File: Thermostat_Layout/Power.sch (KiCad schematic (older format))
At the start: 8 parts, among them J2 Conn_01x02_Male, U3 TSR_1-2433

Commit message: Update schematic
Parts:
- renumbered R5 to R6, R6 to R7, U3 to U4
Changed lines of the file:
@@
 $EndDescr
 $Comp
-L power:+9V #PWR0101
+L power:+9V #PWR02
 U 1 1 5D3E58CF
 P 5500 2750
-F 0 "#PWR0101" H 5500 2600 50  0001 C CNN
+F 0 "#PWR02" H 5500 2600 50  0001 C CNN
 F 1 "+9V" H 5515 2923 50  0000 C CNN
 F 2 "" H 5500 2750 50  0001 C CNN
@@
 Connection ~ 5150 3000
 $Comp
-L Regulator_Switching:TSR_1-2433 U3
+L Regulator_Switching:TSR_1-2433 U4
 U 1 1 5D3E43BD
 P 6050 3100
-F 0 "U3" H 6050 3467 50  0000 C CNN
+F 0 "U4" H 6050 3467 50  0000 C CNN
 F 1 "TSR_1-2433" H 6050 3376 50  0000 C CNN
 F 2 "Converter_DCDC:Converter_DCDC_TRACO_TSR-1_THT" H 6050 2950 50  0001 L CIN
@@
 	5500 2750 5500 3000
 $Comp
-L SparkFun-PowerSymbols:GND #GND0103
+L SparkFun-PowerSymbols:GND #GND09
 U 1 1 5D3ED84A
 P 6050 3400
-F 0 "#GND0103" H 6100 3350 45  0001 L BNN
+F 0 "#GND09" H 6100 3350 45  0001 L BNN
 F 1 "GND" H 6050 3230 45  0000 C CNN
 F 2 "" H 6050 3300 60  0001 C CNN
@@
 	6050 3400 6050 3300
 $Comp
-L SparkFun-PowerSymbols:3.3V #SUPPLY0102
+L SparkFun-PowerSymbols:3.3V #SUPPLY06
 U 1 1 5D3EF310
 P 6600 2750
-F 0 "#SUPPLY0102" H 6650 2750 45  0001 L BNN
+F 0 "#SUPPLY06" H 6650 2750 45  0001 L BNN
 F 1 "3.3V" H 6600 3026 45  0000 C CNN
 F 2 "XXX-00000" H 6600 2931 60  0000 C CNN
@@
 	6600 2750 6600 3000
 $Comp
-L Device:R_US R5
+L Device:R_US R6
 U 1 1 5D3F0E01
 P 5350 4200
-F 0 "R5" H 5418 4246 50  0000 L CNN
+F 0 "R6" H 5418 4246 50  0000 L CNN
 F 1 "220k" H 5418 4155 50  0000 L CNN
 F 2 "Resistor_SMD:R_0402_1005Metric" V 5390 4190 50  0001 C CNN
@@
 $EndComp
 $Comp
-L Device:R_US R6
+L Device:R_US R7
 U 1 1 5D3F14FB
 P 5350 4500
-F 0 "R6" H 5418 4546 50  0000 L CNN
+F 0 "R7" H 5418 4546 50  0000 L CNN
 F 1 "100k" H 5418 4455 50  0000 L CNN
 F 2 "Resistor_SMD:R_0402_1005Metric" V 5390 4490 50  0001 C CNN
@@
 $EndComp
 $Comp
-L power:+9V #PWR0102
+L power:+9V #PWR01
 U 1 1 5D3F1ECA
 P 5350 4000
-F 0 "#PWR0102" H 5350 3850 50  0001 C CNN
+F 0 "#PWR01" H 5350 3850 50  0001 C CNN
 F 1 "+9V" H 5365 4173 50  0000 C CNN
 F 2 "" H 5350 4000 50  0001 C CNN
@@
 $EndComp
 $Comp
-L SparkFun-PowerSymbols:GND #GND0104
+L SparkFun-PowerSymbols:GND #GND08
 U 1 1 5D3F23F7
 P 5350 4700
-F 0 "#GND0104" H 5400 4650 45  0001 L BNN
+F 0 "#GND08" H 5400 4650 45  0001 L BNN
 F 1 "GND" H 5350 4530 45  0000 C CNN
 F 2 "" H 5350 4600 60  0001 C CNN

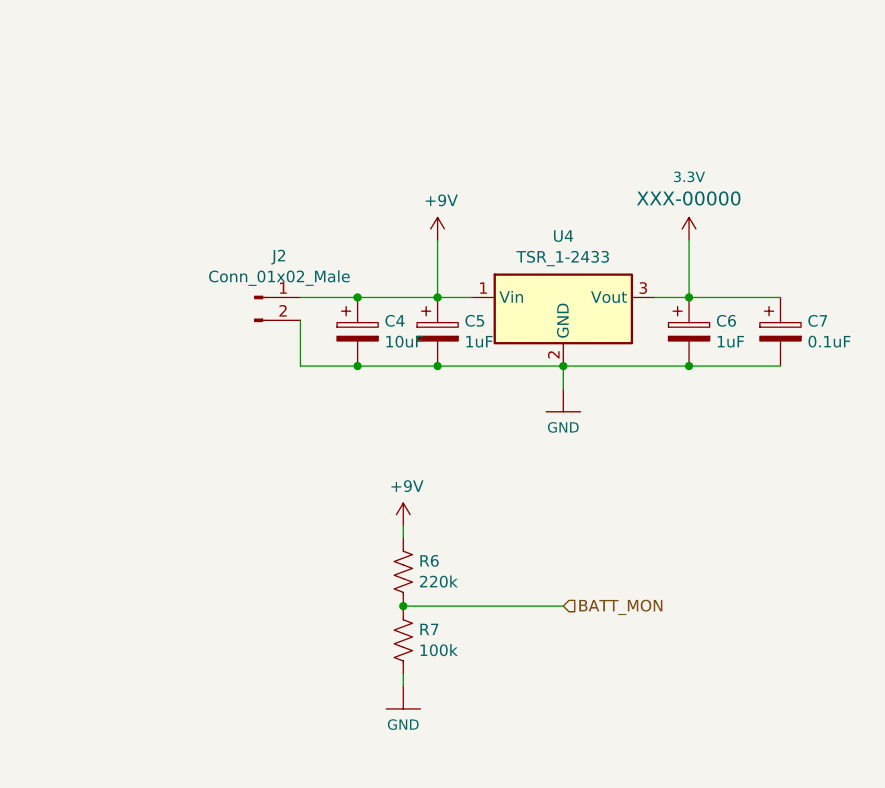
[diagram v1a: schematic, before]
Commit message: FInalize schematic for thermostat
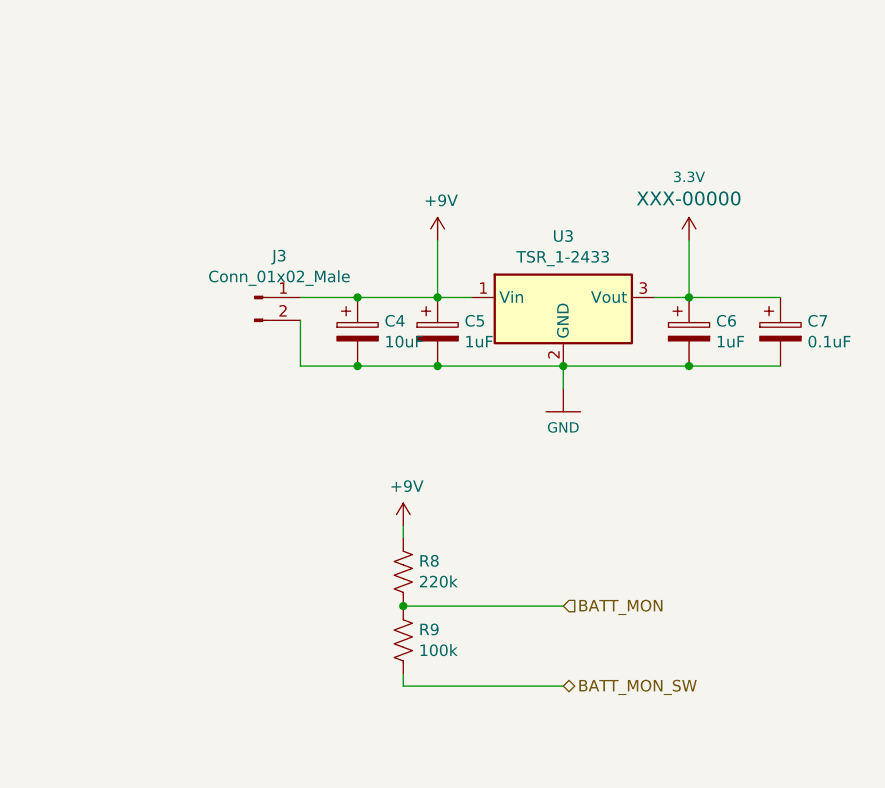
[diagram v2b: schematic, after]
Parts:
- renumbered J2 to J3, R6 to R8, R7 to R9, U4 to U3
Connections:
- net GND: no longer R9.2
- new net BATT_MON_SW: R9.2
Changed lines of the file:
@@
 $EndComp
 $Comp
-L Connector:Conn_01x02_Male J2
+L Connector:Conn_01x02_Male J3
 U 1 1 5D3E6F45
 P 4700 3000
-F 0 "J2" H 4808 3181 50  0000 C CNN
+F 0 "J3" H 4808 3181 50  0000 C CNN
 F 1 "Conn_01x02_Male" H 4808 3090 50  0000 C CNN
 F 2 "Connector_JST:JST_PH_S2B-PH-SM4-TB_1x02-1MP_P2.00mm_Horizontal" H 4700 3000 50  0001 C CNN
@@
 Connection ~ 5150 3000
 $Comp
-L Regulator_Switching:TSR_1-2433 U4
+L Regulator_Switching:TSR_1-2433 U3
 U 1 1 5D3E43BD
 P 6050 3100
-F 0 "U4" H 6050 3467 50  0000 C CNN
+F 0 "U3" H 6050 3467 50  0000 C CNN
 F 1 "TSR_1-2433" H 6050 3376 50  0000 C CNN
 F 2 "Converter_DCDC:Converter_DCDC_TRACO_TSR-1_THT" H 6050 2950 50  0001 L CIN
@@
 	5500 2750 5500 3000
 $Comp
-L SparkFun-PowerSymbols:GND #GND09
+L SparkFun-PowerSymbols:GND #GND07
 U 1 1 5D3ED84A
 P 6050 3400
-F 0 "#GND09" H 6100 3350 45  0001 L BNN
+F 0 "#GND07" H 6100 3350 45  0001 L BNN
 F 1 "GND" H 6050 3230 45  0000 C CNN
 F 2 "" H 6050 3300 60  0001 C CNN
@@
 	6050 3400 6050 3300
 $Comp
-L SparkFun-PowerSymbols:3.3V #SUPPLY06
+L SparkFun-PowerSymbols:3.3V #SUPPLY05
 U 1 1 5D3EF310
 P 6600 2750
-F 0 "#SUPPLY06" H 6650 2750 45  0001 L BNN
+F 0 "#SUPPLY05" H 6650 2750 45  0001 L BNN
 F 1 "3.3V" H 6600 3026 45  0000 C CNN
 F 2 "XXX-00000" H 6600 2931 60  0000 C CNN
@@
 	6600 2750 6600 3000
 $Comp
-L Device:R_US R6
+L Device:R_US R8
 U 1 1 5D3F0E01
 P 5350 4200
-F 0 "R6" H 5418 4246 50  0000 L CNN
+F 0 "R8" H 5418 4246 50  0000 L CNN
 F 1 "220k" H 5418 4155 50  0000 L CNN
 F 2 "Resistor_SMD:R_0402_1005Metric" V 5390 4190 50  0001 C CNN
@@
 $EndComp
 $Comp
-L Device:R_US R7
+L Device:R_US R9
 U 1 1 5D3F14FB
 P 5350 4500
-F 0 "R7" H 5418 4546 50  0000 L CNN
+F 0 "R9" H 5418 4546 50  0000 L CNN
 F 1 "100k" H 5418 4455 50  0000 L CNN
 F 2 "Resistor_SMD:R_0402_1005Metric" V 5390 4490 50  0001 C CNN
@@
 	1    0    0    -1
 $EndComp
-$Comp
-L SparkFun-PowerSymbols:GND #GND08
-U 1 1 5D3F23F7
-P 5350 4700
-F 0 "#GND08" H 5400 4650 45  0001 L BNN
-F 1 "GND" H 5350 4530 45  0000 C CNN
-F 2 "" H 5350 4600 60  0001 C CNN
-F 3 "" H 5350 4600 60  0001 C CNN
-	1    5350 4700
-	1    0    0    -1
-$EndComp
 Wire Wire Line
 	5350 4000 5350 4050
@@
 Text HLabel 6050 4350 2    50   Input ~ 0
 BATT_MON
+Text HLabel 6050 4700 2    50   3State ~ 0
+BATT_MON_SW
+Wire Wire Line
+	6050 4700 5350 4700
 $EndSCHEMATC

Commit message: Schematic and PCB layout for thermostat
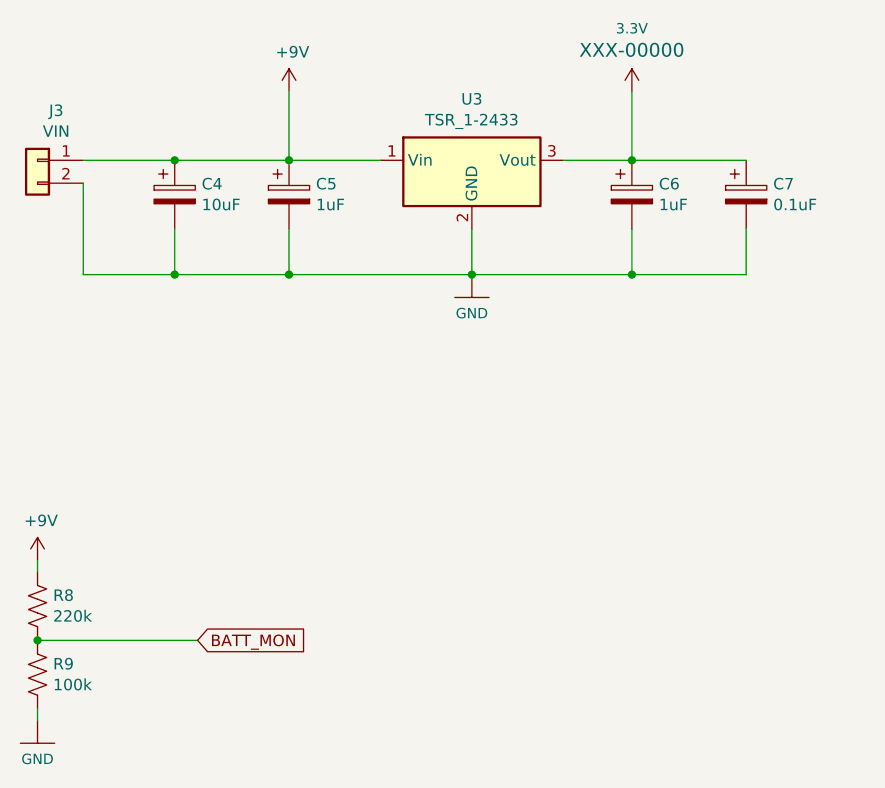
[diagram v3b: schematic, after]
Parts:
- removed J3: Conn_01x02_Male, Connector_JST:JST_PH_S2B-PH-SM4-TB_1x02-1MP_P2.00mm_Horizontal, symbol Connector:Conn_01x02_Male
- added J3: VIN, Connector_JST:JST_PH_S2B-PH-SM4-TB_1x02-1MP_P2.00mm_Horizontal, symbol Connector_Generic:Conn_01x02
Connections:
- net BATT_MON_SW is gone; now on net GND: R9.2
- net +9V: now also J3.1 (Pin_1)
- net GND: now also J3.2 (Pin_2)
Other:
- moved on the sheet: C4, C5, C6, C7, R8, R9
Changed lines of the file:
@@
 L power:+9V #PWR02
 U 1 1 5D3E58CF
-P 5500 2750
-F 0 "#PWR02" H 5500 2600 50  0001 C CNN
-F 1 "+9V" H 5515 2923 50  0000 C CNN
-F 2 "" H 5500 2750 50  0001 C CNN
-F 3 "" H 5500 2750 50  0001 C CNN
-	1    5500 2750
+P 4850 2100
+F 0 "#PWR02" H 4850 1950 50  0001 C CNN
+F 1 "+9V" H 4865 2273 50  0000 C CNN
+F 2 "" H 4850 2100 50  0001 C CNN
+F 3 "" H 4850 2100 50  0001 C CNN
+	1    4850 2100
 	1    0    0    -1
 $EndComp
 $Comp
-L Connector:Conn_01x02_Male J3
-U 1 1 5D3E6F45
-P 4700 3000
-F 0 "J3" H 4808 3181 50  0000 C CNN
-F 1 "Conn_01x02_Male" H 4808 3090 50  0000 C CNN
-F 2 "Connector_JST:JST_PH_S2B-PH-SM4-TB_1x02-1MP_P2.00mm_Horizontal" H 4700 3000 50  0001 C CNN
-F 3 "~" H 4700 3000 50  0001 C CNN
-	1    4700 3000
-	1    0    0    -1
-$EndComp
-Wire Wire Line
-	4900 3000 5150 3000
-$Comp
 L Device:CP C4
 U 1 1 5D3EA330
-P 5150 3150
-F 0 "C4" H 5268 3196 50  0000 L CNN
-F 1 "10uF" H 5268 3105 50  0000 L CNN
-F 2 "Capacitor_SMD:C_0402_1005Metric" H 5188 3000 50  0001 C CNN
-F 3 "~" H 5150 3150 50  0001 C CNN
-	1    5150 3150
-	1    0    0    -1
-$EndComp
-Connection ~ 5150 3000
-$Comp
-L Regulator_Switching:TSR_1-2433 U3
-U 1 1 5D3E43BD
-P 6050 3100
-F 0 "U3" H 6050 3467 50  0000 C CNN
-F 1 "TSR_1-2433" H 6050 3376 50  0000 C CNN
-F 2 "Converter_DCDC:Converter_DCDC_TRACO_TSR-1_THT" H 6050 2950 50  0001 L CIN
-F 3 "http://www.tracopower.com/products/tsr1.pdf" H 6050 3100 50  0001 C CNN
-	1    6050 3100
+P 4350 2550
+F 0 "C4" H 4468 2596 50  0000 L CNN
+F 1 "10uF" H 4468 2505 50  0000 L CNN
+F 2 "Capacitor_SMD:C_0402_1005Metric" H 4388 2400 50  0001 C CNN
+F 3 "~" H 4350 2550 50  0001 C CNN
+	1    4350 2550
 	1    0    0    -1
 $EndComp
@@
 L Device:CP C5
 U 1 1 5D3EBB10
-P 5500 3150
-F 0 "C5" H 5618 3196 50  0000 L CNN
-F 1 "1uF" H 5618 3105 50  0000 L CNN
-F 2 "Capacitor_SMD:C_0402_1005Metric" H 5538 3000 50  0001 C CNN
-F 3 "~" H 5500 3150 50  0001 C CNN
-	1    5500 3150
+P 4850 2550
+F 0 "C5" H 4968 2596 50  0000 L CNN
+F 1 "1uF" H 4968 2505 50  0000 L CNN
+F 2 "Capacitor_SMD:C_0402_1005Metric" H 4888 2400 50  0001 C CNN
+F 3 "~" H 4850 2550 50  0001 C CNN
+	1    4850 2550
 	1    0    0    -1
 $EndComp
-Connection ~ 5500 3000
-Wire Wire Line
-	5500 3000 5650 3000
-Wire Wire Line
-	4900 3100 4900 3300
-Wire Wire Line
-	4900 3300 5150 3300
-Wire Wire Line
-	5150 3300 5500 3300
-Connection ~ 5150 3300
-Wire Wire Line
-	5500 3300 6050 3300
-Connection ~ 5500 3300
-Wire Wire Line
-	5150 3000 5500 3000
-Wire Wire Line
-	5500 2750 5500 3000
 $Comp
 L SparkFun-PowerSymbols:GND #GND07
 U 1 1 5D3ED84A
-P 6050 3400
-F 0 "#GND07" H 6100 3350 45  0001 L BNN
-F 1 "GND" H 6050 3230 45  0000 C CNN
-F 2 "" H 6050 3300 60  0001 C CNN
-F 3 "" H 6050 3300 60  0001 C CNN
-	1    6050 3400
+P 5650 2900
+F 0 "#GND07" H 5700 2850 45  0001 L BNN
+F 1 "GND" H 5650 2730 45  0000 C CNN
+F 2 "" H 5650 2800 60  0001 C CNN
+F 3 "" H 5650 2800 60  0001 C CNN
+	1    5650 2900
 	1    0    0    -1
 $EndComp
@@
 L Device:CP C6
 U 1 1 5D3EDD28
-P 6600 3150
-F 0 "C6" H 6718 3196 50  0000 L CNN
-F 1 "1uF" H 6718 3105 50  0000 L CNN
-F 2 "Capacitor_SMD:C_0402_1005Metric" H 6638 3000 50  0001 C CNN
-F 3 "~" H 6600 3150 50  0001 C CNN
-	1    6600 3150
+P 6350 2550
+F 0 "C6" H 6468 2596 50  0000 L CNN
+F 1 "1uF" H 6468 2505 50  0000 L CNN
+F 2 "Capacitor_SMD:C_0402_1005Metric" H 6388 2400 50  0001 C CNN
+F 3 "~" H 6350 2550 50  0001 C CNN
+	1    6350 2550
 	1    0    0    -1
 $EndComp
@@
 L Device:CP C7
 U 1 1 5D3EE418
-P 7000 3150
-F 0 "C7" H 7118 3196 50  0000 L CNN
-F 1 "0.1uF" H 7118 3105 50  0000 L CNN
-F 2 "Capacitor_SMD:C_0402_1005Metric" H 7038 3000 50  0001 C CNN
-F 3 "~" H 7000 3150 50  0001 C CNN
-	1    7000 3150
+P 6850 2550
+F 0 "C7" H 6968 2596 50  0000 L CNN
+F 1 "0.1uF" H 6968 2505 50  0000 L CNN
+F 2 "Capacitor_SMD:C_0402_1005Metric" H 6888 2400 50  0001 C CNN
+F 3 "~" H 6850 2550 50  0001 C CNN
+	1    6850 2550
 	1    0    0    -1
 $EndComp
-Wire Wire Line
-	6050 3300 6600 3300
-Connection ~ 6050 3300
-Wire Wire Line
-	6600 3300 7000 3300
-Connection ~ 6600 3300
-Wire Wire Line
-	6450 3000 6600 3000
-Wire Wire Line
-	6600 3000 7000 3000
-Connection ~ 6600 3000
-Wire Wire Line
-	6050 3400 6050 3300
 $Comp
 L SparkFun-PowerSymbols:3.3V #SUPPLY05
 U 1 1 5D3EF310
-P 6600 2750
-F 0 "#SUPPLY05" H 6650 2750 45  0001 L BNN
-F 1 "3.3V" H 6600 3026 45  0000 C CNN
-F 2 "XXX-00000" H 6600 2931 60  0000 C CNN
-F 3 "" H 6600 2750 60  0001 C CNN
-	1    6600 2750
+P 6350 2100
+F 0 "#SUPPLY05" H 6400 2100 45  0001 L BNN
+F 1 "3.3V" H 6350 2376 45  0000 C CNN
+F 2 "XXX-00000" H 6350 2281 60  0000 C CNN
+F 3 "" H 6350 2100 60  0001 C CNN
+	1    6350 2100
 	1    0    0    -1
 $EndComp
-Wire Wire Line
-	6600 2750 6600 3000
 $Comp
 L Device:R_US R8
 U 1 1 5D3F0E01
-P 5350 4200
-F 0 "R8" H 5418 4246 50  0000 L CNN
-F 1 "220k" H 5418 4155 50  0000 L CNN
-F 2 "Resistor_SMD:R_0402_1005Metric" V 5390 4190 50  0001 C CNN
-F 3 "~" H 5350 4200 50  0001 C CNN
-	1    5350 4200
+P 3750 4350
+F 0 "R8" H 3818 4396 50  0000 L CNN
+F 1 "220k" H 3818 4305 50  0000 L CNN
+F 2 "Resistor_SMD:R_0402_1005Metric" V 3790 4340 50  0001 C CNN
+F 3 "~" H 3750 4350 50  0001 C CNN
+	1    3750 4350
 	1    0    0    -1
 $EndComp
@@
 L Device:R_US R9
 U 1 1 5D3F14FB
-P 5350 4500
-F 0 "R9" H 5418 4546 50  0000 L CNN
-F 1 "100k" H 5418 4455 50  0000 L CNN
-F 2 "Resistor_SMD:R_0402_1005Metric" V 5390 4490 50  0001 C CNN
-F 3 "~" H 5350 4500 50  0001 C CNN
-	1    5350 4500
+P 3750 4650
+F 0 "R9" H 3818 4696 50  0000 L CNN
+F 1 "100k" H 3818 4605 50  0000 L CNN
+F 2 "Resistor_SMD:R_0402_1005Metric" V 3790 4640 50  0001 C CNN
+F 3 "~" H 3750 4650 50  0001 C CNN
+	1    3750 4650
 	1    0    0    -1
 $EndComp
@@
 L power:+9V #PWR01
 U 1 1 5D3F1ECA
-P 5350 4000
-F 0 "#PWR01" H 5350 3850 50  0001 C CNN
-F 1 "+9V" H 5365 4173 50  0000 C CNN
-F 2 "" H 5350 4000 50  0001 C CNN
-F 3 "" H 5350 4000 50  0001 C CNN
-	1    5350 4000
+P 3750 4150
+F 0 "#PWR01" H 3750 4000 50  0001 C CNN
+F 1 "+9V" H 3765 4323 50  0000 C CNN
+F 2 "" H 3750 4150 50  0001 C CNN
+F 3 "" H 3750 4150 50  0001 C CNN
+	1    3750 4150
 	1    0    0    -1
 $EndComp
 Wire Wire Line
-	5350 4000 5350 4050
+	3750 4150 3750 4200
 Wire Wire Line
-	5350 4650 5350 4700
+	3750 4800 3750 4850
 Wire Wire Line
-	5350 4350 6050 4350
-Connection ~ 5350 4350
-Text HLabel 6050 4350 2    50   Input ~ 0
+	3750 4500 4450 4500
+Connection ~ 3750 4500
+Wire Wire Line
+	4350 2400 4850 2400
+Connection ~ 4850 2400
+Wire Wire Line
+	4850 2100 4850 2400
+Wire Wire Line
+	6350 2400 6850 2400
+Connection ~ 6350 2400
+Wire Wire Line
+	4350 2700 4350 2900
+Wire Wire Line
+	4350 2900 4850 2900
+Wire Wire Line
+	6850 2900 6850 2700
+Wire Wire Line
+	6350 2700 6350 2900
+Wire Wire Line
+	6350 2900 6850 2900
+Wire Wire Line
+	4850 2700 4850 2900
+Wire Wire Line
+	6350 2100 6350 2400
+Wire Wire Line
+	3950 2400 4350 2400
+Connection ~ 4350 2400
+Wire Wire Line
+	3950 2900 4350 2900
+Connection ~ 4350 2900
+$Comp
+L Regulator_Switching:TSR_1-2433 U3
+U 1 1 5DB81056
+P 5650 2500
+F 0 "U3" H 5650 2867 50  0000 C CNN
+F 1 "TSR_1-2433" H 5650 2776 50  0000 C CNN
+F 2 "Converter_DCDC:Converter_DCDC_TRACO_TSR-1_THT" H 5650 2350 50  0001 L CIN
+F 3 "http://www.tracopower.com/products/tsr1.pdf" H 5650 2500 50  0001 C CNN
+	1    5650 2500
+	1    0    0    -1
+$EndComp
+Wire Wire Line
+	5650 2700 5650 2900
+Wire Wire Line
+	4850 2900 5650 2900
+Connection ~ 4850 2900
+Connection ~ 5650 2900
+Wire Wire Line
+	6350 2900 5650 2900
+Connection ~ 6350 2900
+Wire Wire Line
+	4850 2400 5250 2400
+Wire Wire Line
+	6050 2400 6350 2400
+Wire Wire Line
+	3950 2500 3950 2900
+$Comp
+L Connector_Generic:Conn_01x02 J3
+U 1 1 5DBA4D6C
+P 3750 2400
+F 0 "J3" H 3668 2617 50  0000 C CNN
+F 1 "VIN" H 3668 2526 50  0000 C CNN
+F 2 "Connector_JST:JST_PH_S2B-PH-SM4-TB_1x02-1MP_P2.00mm_Horizontal" H 3750 2400 50  0001 C CNN
+F 3 "~" H 3750 2400 50  0001 C CNN
+	1    3750 2400
+	-1   0    0    -1
+$EndComp
+$Comp
+L SparkFun-PowerSymbols:GND #GND0101
+U 1 1 5DB78E1E
+P 3750 4850
+F 0 "#GND0101" H 3800 4800 45  0001 L BNN
+F 1 "GND" H 3750 4680 45  0000 C CNN
+F 2 "" H 3750 4750 60  0001 C CNN
+F 3 "" H 3750 4750 60  0001 C CNN
+	1    3750 4850
+	1    0    0    -1
+$EndComp
+Text GLabel 4450 4500 2    50   Input ~ 0
 BATT_MON
-Text HLabel 6050 4700 2    50   3State ~ 0
-BATT_MON_SW
-Wire Wire Line
-	6050 4700 5350 4700
 $EndSCHEMATC
